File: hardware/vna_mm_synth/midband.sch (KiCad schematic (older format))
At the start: 6 parts

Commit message: added power supply sequencing
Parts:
- gave numbers to parts that had none: 6
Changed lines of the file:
@@
 $EndDescr
 $Comp
-L maam-011101:MAAM-011101 U?
+L maam-011101:MAAM-011101 U601
 U 1 1 5D2874FF
 P 3650 3850
-F 0 "U?" V 4100 4100 60  0000 C CNN
+F 0 "U601" V 4100 4100 60  0000 C CNN
 F 1 "MAAM-011101" V 4000 4350 60  0000 C CNN
 F 2 "" H 3800 3750 60  0000 C CNN
@@
 $EndComp
 $Comp
-L power:GND #PWR?
+L power:GND #PWR0148
 U 1 1 5D2E3704
 P 3100 3850
-F 0 "#PWR?" H 3100 3600 50  0001 C CNN
+F 0 "#PWR0148" H 3100 3600 50  0001 C CNN
 F 1 "GND" H 3105 3677 50  0000 C CNN
 F 2 "" H 3100 3850 50  0001 C CNN
@@
 	3100 3850 3200 3850
 $Comp
-L power:GND #PWR?
+L power:GND #PWR0149
 U 1 1 5D2FD268
 P 3650 3300
-F 0 "#PWR?" H 3650 3050 50  0001 C CNN
+F 0 "#PWR0149" H 3650 3050 50  0001 C CNN
 F 1 "GND" H 3655 3127 50  0000 C CNN
 F 2 "" H 3650 3300 50  0001 C CNN
@@
 	3550 3350 3550 3400
 $Comp
-L power:GND #PWR?
+L power:GND #PWR0150
 U 1 1 5D2FE136
 P 3650 4400
-F 0 "#PWR?" H 3650 4150 50  0001 C CNN
+F 0 "#PWR0150" H 3650 4150 50  0001 C CNN
 F 1 "GND" H 3655 4227 50  0000 C CNN
 F 2 "" H 3650 4400 50  0001 C CNN
@@
 	3550 4300 3550 4400
 $Comp
-L Device:L_Small L?
+L Device:L_Small L601
 U 1 1 5D2FEAD5
 P 4550 3900
-F 0 "L?" H 4598 3946 50  0000 L CNN
+F 0 "L601" H 4598 3946 50  0000 L CNN
 F 1 "BLM15GG471" H 4598 3855 50  0000 L CNN
 F 2 "" H 4550 3900 50  0001 C CNN
@@
 INTERNAL DC BLOCK\nON RFin
 $Comp
-L Device:C_Small C?
+L Device:C_Small C601
 U 1 1 5D2FFB44
 P 5100 4400
-F 0 "C?" V 4871 4400 50  0000 C CNN
+F 0 "C601" V 4871 4400 50  0000 C CNN
 F 1 "100 pF" V 4962 4400 50  0000 C CNN
 F 2 "" H 5100 4400 50  0001 C CNN
@@
 Connection ~ 4550 4400
 $Comp
-L Device:C_Small C?
+L Device:C_Small C602
 U 1 1 5D3002AC
 P 5150 3450
-F 0 "C?" H 5058 3404 50  0000 R CNN
+F 0 "C602" H 5058 3404 50  0000 R CNN
 F 1 "100 pF" H 5058 3495 50  0000 R CNN
 F 2 "" H 5150 3450 50  0001 C CNN
@@
 $EndComp
 $Comp
-L Device:C_Small C?
+L Device:C_Small C603
 U 1 1 5D301255
 P 5600 3450
-F 0 "C?" H 5508 3404 50  0000 R CNN
+F 0 "C603" H 5508 3404 50  0000 R CNN
 F 1 "100 nF" H 5508 3495 50  0000 R CNN
 F 2 "" H 5600 3450 50  0001 C CNN
@@
 $EndComp
 $Comp
-L Device:C_Small C?
+L Device:C_Small C604
 U 1 1 5D3015C8
 P 6050 3450
-F 0 "C?" H 5958 3404 50  0000 R CNN
+F 0 "C604" H 5958 3404 50  0000 R CNN
 F 1 "2.2 uF" H 5958 3495 50  0000 R CNN
 F 2 "" H 6050 3450 50  0001 C CNN
@@
 $EndComp
 $Comp
-L power:GND #PWR?
+L power:GND #PWR0151
 U 1 1 5D301FA8
 P 5150 3600
-F 0 "#PWR?" H 5150 3350 50  0001 C CNN
+F 0 "#PWR0151" H 5150 3350 50  0001 C CNN
 F 1 "GND" H 5155 3427 50  0000 C CNN
 F 2 "" H 5150 3600 50  0001 C CNN
@@
 	5150 3550 5150 3600
 $Comp
-L power:GND #PWR?
+L power:GND #PWR0152
 U 1 1 5D30289B
 P 5600 3600
-F 0 "#PWR?" H 5600 3350 50  0001 C CNN
+F 0 "#PWR0152" H 5600 3350 50  0001 C CNN
 F 1 "GND" H 5605 3427 50  0000 C CNN
 F 2 "" H 5600 3600 50  0001 C CNN
@@
 	5600 3550 5600 3600
 $Comp
-L power:GND #PWR?
+L power:GND #PWR0153
 U 1 1 5D302DE5
 P 6050 3600
-F 0 "#PWR?" H 6050 3350 50  0001 C CNN
+F 0 "#PWR0153" H 6050 3350 50  0001 C CNN
 F 1 "GND" H 6055 3427 50  0000 C CNN
 F 2 "" H 6050 3600 50  0001 C CNN

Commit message: added trl cal and set of breakout boards
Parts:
- C601, C602, C603: footprint (none) -> Capacitors_SMD:C_0402
- C604: footprint (none) -> Capacitors_SMD:C_0603
- L601: footprint (none) -> Resistors_SMD:R_0402
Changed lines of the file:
@@
 F 0 "U601" V 4100 4100 60  0000 C CNN
 F 1 "MAAM-011101" V 4000 4350 60  0000 C CNN
-F 2 "" H 3800 3750 60  0000 C CNN
+F 2 "" H 3800 3750 60  0001 C CNN
 F 3 "" H 3800 3750 60  0000 C CNN
 	1    3650 3850
@@
 $EndComp
 $Comp
-L power:GND #PWR0148
+L power:GND #PWR0601
 U 1 1 5D2E3704
 P 3100 3850
-F 0 "#PWR0148" H 3100 3600 50  0001 C CNN
+F 0 "#PWR0601" H 3100 3600 50  0001 C CNN
 F 1 "GND" H 3105 3677 50  0000 C CNN
 F 2 "" H 3100 3850 50  0001 C CNN
@@
 	3100 3850 3200 3850
 $Comp
-L power:GND #PWR0149
+L power:GND #PWR0602
 U 1 1 5D2FD268
 P 3650 3300
-F 0 "#PWR0149" H 3650 3050 50  0001 C CNN
+F 0 "#PWR0602" H 3650 3050 50  0001 C CNN
 F 1 "GND" H 3655 3127 50  0000 C CNN
 F 2 "" H 3650 3300 50  0001 C CNN
@@
 	3550 3350 3550 3400
 $Comp
-L power:GND #PWR0150
+L power:GND #PWR0603
 U 1 1 5D2FE136
 P 3650 4400
-F 0 "#PWR0150" H 3650 4150 50  0001 C CNN
+F 0 "#PWR0603" H 3650 4150 50  0001 C CNN
 F 1 "GND" H 3655 4227 50  0000 C CNN
 F 2 "" H 3650 4400 50  0001 C CNN
@@
 F 0 "L601" H 4598 3946 50  0000 L CNN
 F 1 "BLM15GG471" H 4598 3855 50  0000 L CNN
-F 2 "" H 4550 3900 50  0001 C CNN
+F 2 "Resistors_SMD:R_0402" H 4550 3900 50  0001 C CNN
 F 3 "~" H 4550 3900 50  0001 C CNN
 	1    4550 3900
@@
 F 0 "C601" V 4871 4400 50  0000 C CNN
 F 1 "100 pF" V 4962 4400 50  0000 C CNN
-F 2 "" H 5100 4400 50  0001 C CNN
+F 2 "Capacitors_SMD:C_0402" H 5100 4400 50  0001 C CNN
 F 3 "~" H 5100 4400 50  0001 C CNN
 	1    5100 4400
@@
 F 0 "C602" H 5058 3404 50  0000 R CNN
 F 1 "100 pF" H 5058 3495 50  0000 R CNN
-F 2 "" H 5150 3450 50  0001 C CNN
+F 2 "Capacitors_SMD:C_0402" H 5150 3450 50  0001 C CNN
 F 3 "~" H 5150 3450 50  0001 C CNN
 	1    5150 3450
@@
 F 0 "C603" H 5508 3404 50  0000 R CNN
 F 1 "100 nF" H 5508 3495 50  0000 R CNN
-F 2 "" H 5600 3450 50  0001 C CNN
+F 2 "Capacitors_SMD:C_0402" H 5600 3450 50  0001 C CNN
 F 3 "~" H 5600 3450 50  0001 C CNN
 	1    5600 3450
@@
 F 0 "C604" H 5958 3404 50  0000 R CNN
 F 1 "2.2 uF" H 5958 3495 50  0000 R CNN
-F 2 "" H 6050 3450 50  0001 C CNN
+F 2 "Capacitors_SMD:C_0603" H 6050 3450 50  0001 C CNN
 F 3 "~" H 6050 3450 50  0001 C CNN
 	1    6050 3450
@@
 $EndComp
 $Comp
-L power:GND #PWR0151
+L power:GND #PWR0604
 U 1 1 5D301FA8
 P 5150 3600
-F 0 "#PWR0151" H 5150 3350 50  0001 C CNN
+F 0 "#PWR0604" H 5150 3350 50  0001 C CNN
 F 1 "GND" H 5155 3427 50  0000 C CNN
 F 2 "" H 5150 3600 50  0001 C CNN
@@
 	5150 3550 5150 3600
 $Comp
-L power:GND #PWR0152
+L power:GND #PWR0605
 U 1 1 5D30289B
 P 5600 3600
-F 0 "#PWR0152" H 5600 3350 50  0001 C CNN
+F 0 "#PWR0605" H 5600 3350 50  0001 C CNN
 F 1 "GND" H 5605 3427 50  0000 C CNN
 F 2 "" H 5600 3600 50  0001 C CNN
@@
 	5600 3550 5600 3600
 $Comp
-L power:GND #PWR0153
+L power:GND #PWR0606
 U 1 1 5D302DE5
 P 6050 3600
-F 0 "#PWR0153" H 6050 3350 50  0001 C CNN
+F 0 "#PWR0606" H 6050 3350 50  0001 C CNN
 F 1 "GND" H 6055 3427 50  0000 C CNN
 F 2 "" H 6050 3600 50  0001 C CNN

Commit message: fixed mirrored 3.3V regulator on sequencer board, created and assigned footprints for synth
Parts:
- U601: footprint (none) -> vna_mm:TDFN6
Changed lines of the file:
@@
 F 0 "U601" V 4100 4100 60  0000 C CNN
 F 1 "MAAM-011101" V 4000 4350 60  0000 C CNN
-F 2 "" H 3800 3750 60  0001 C CNN
+F 2 "vna_mm:TDFN6" H 3800 3750 60  0001 C CNN
 F 3 "" H 3800 3750 60  0000 C CNN
 	1    3650 3850

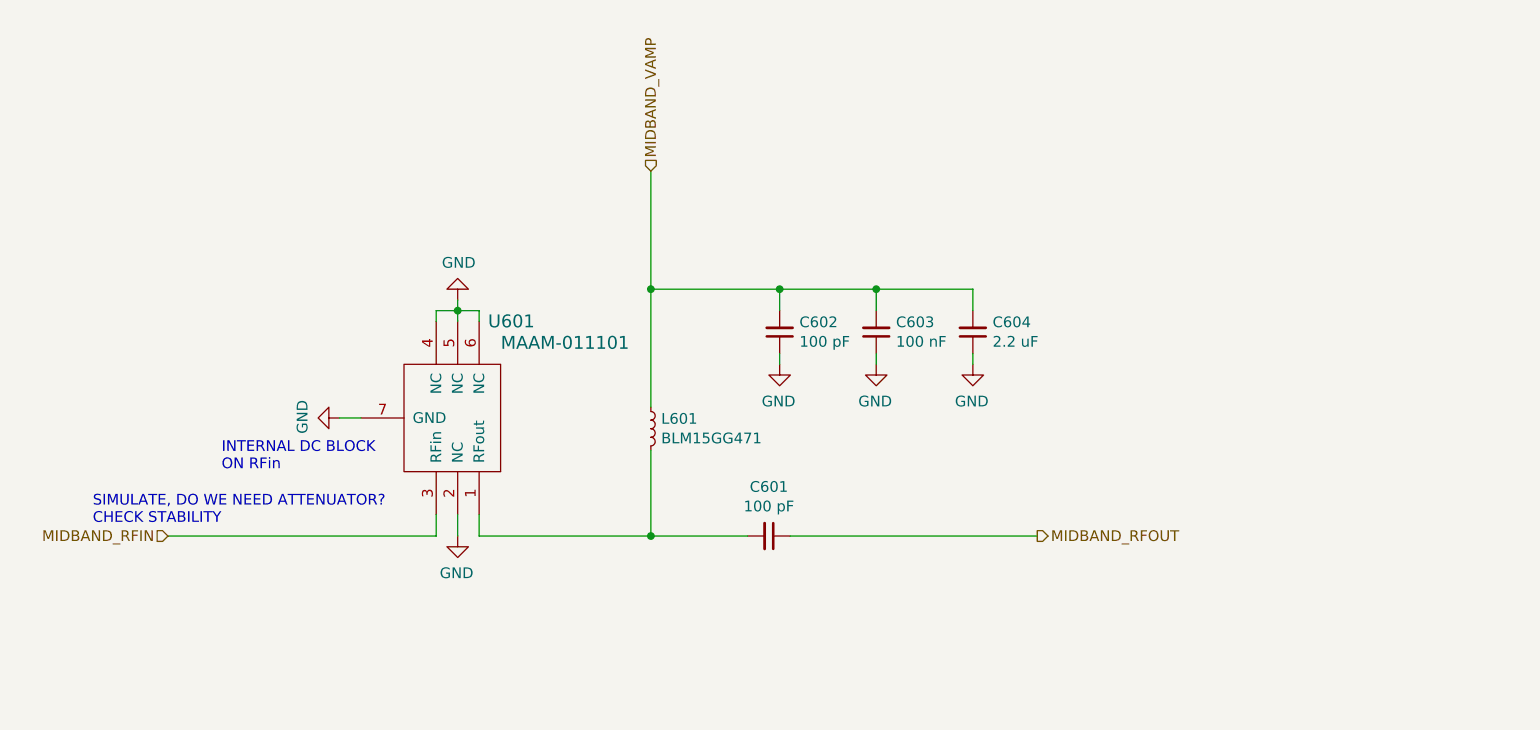
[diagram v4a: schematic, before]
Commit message: started separate reference clock generation board
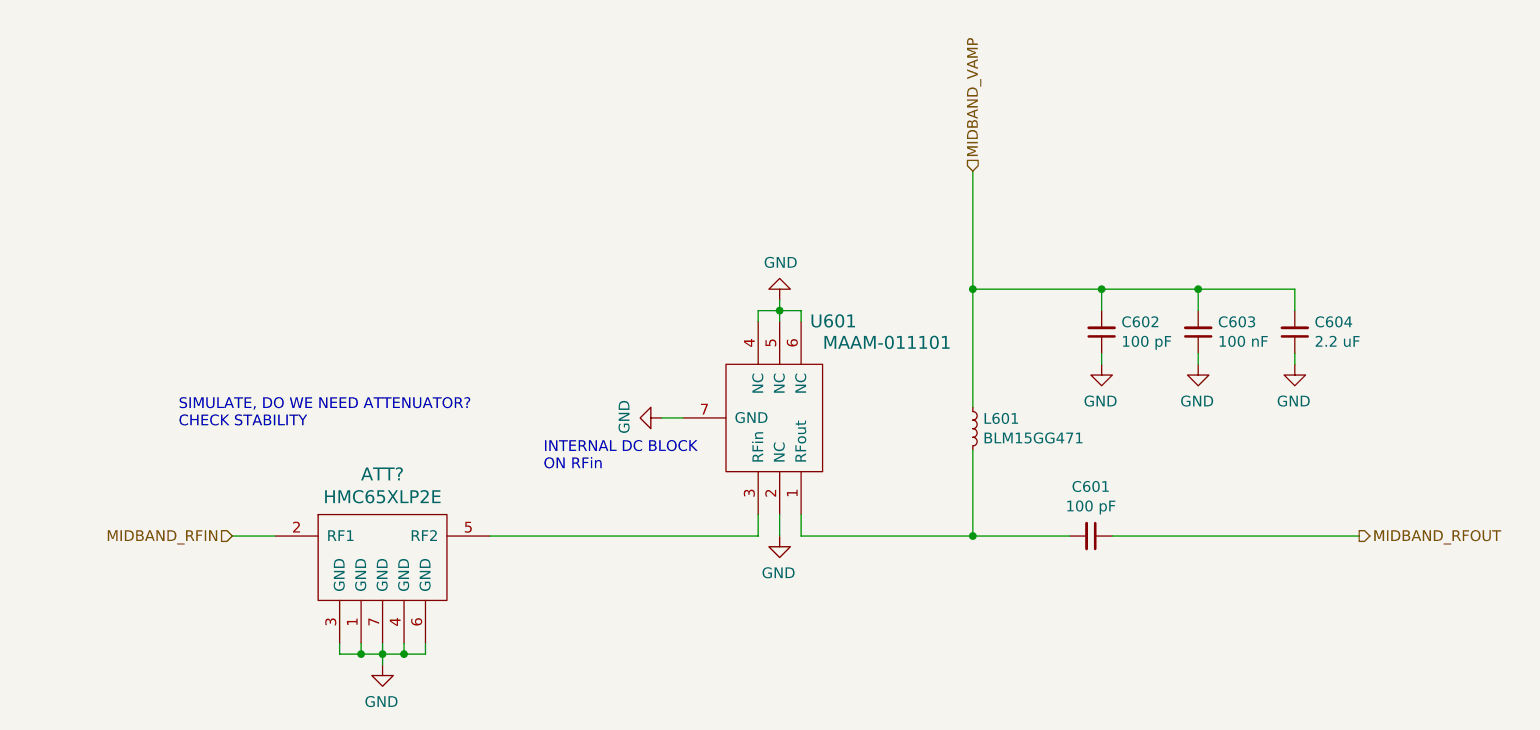
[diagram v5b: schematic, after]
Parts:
- added ATT?: HMC65XLP2E, vna_mm:LP2E_DFN6_2x2mm_Pitch0.60mm, symbol vna_mm:HMC65XLP2E
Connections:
- net GND: now also ATT?.1 (GND), ATT?.3 (GND), ATT?.4 (GND), ATT?.6 (GND), ATT?.7 (GND)
- net MIDBAND_RFIN: now also ATT?.2 (RF1); no longer U601.3 (RFin)
- new net: ATT?.5 (RF2), U601.3 (RFin)
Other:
- moved on the sheet: C601, C602, C603, C604, L601, U601

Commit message: cleanup and update vna mm synth schematic for modern kicad libraries
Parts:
- C601, C602, C603: footprint Capacitors_SMD:C_0402 -> Capacitor_SMD:C_0402_1005Metric
- C604: footprint Capacitors_SMD:C_0603 -> Capacitor_SMD:C_0603_1608Metric
- L601: footprint Resistors_SMD:R_0402 -> Inductor_SMD:L_0402_1005Metric
- U601: symbol maam-011101:MAAM-011101 -> vna_mm:MAAM-011101
- gave numbers to parts that had none: 1
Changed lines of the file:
@@
 $Descr A4 11693 8268
 encoding utf-8
-Sheet 6 12
+Sheet 6 11
 Title ""
 Date ""
@@
 $EndDescr
 $Comp
-L maam-011101:MAAM-011101 U601
+L vna_mm:MAAM-011101 U601
 U 1 1 5D2874FF
 P 5150 3850
@@
 F 0 "L601" H 6098 3946 50  0000 L CNN
 F 1 "BLM15GG471" H 6098 3855 50  0000 L CNN
-F 2 "Resistors_SMD:R_0402" H 6050 3900 50  0001 C CNN
+F 2 "Inductor_SMD:L_0402_1005Metric" H 6050 3900 50  0001 C CNN
 F 3 "~" H 6050 3900 50  0001 C CNN
 	1    6050 3900
@@
 F 0 "C601" V 6371 4400 50  0000 C CNN
 F 1 "100 pF" V 6462 4400 50  0000 C CNN
-F 2 "Capacitors_SMD:C_0402" H 6600 4400 50  0001 C CNN
+F 2 "Capacitor_SMD:C_0402_1005Metric" H 6600 4400 50  0001 C CNN
 F 3 "~" H 6600 4400 50  0001 C CNN
 	1    6600 4400
@@
 F 0 "C602" H 6558 3404 50  0000 R CNN
 F 1 "100 pF" H 6558 3495 50  0000 R CNN
-F 2 "Capacitors_SMD:C_0402" H 6650 3450 50  0001 C CNN
+F 2 "Capacitor_SMD:C_0402_1005Metric" H 6650 3450 50  0001 C CNN
 F 3 "~" H 6650 3450 50  0001 C CNN
 	1    6650 3450
@@
 F 0 "C603" H 7008 3404 50  0000 R CNN
 F 1 "100 nF" H 7008 3495 50  0000 R CNN
-F 2 "Capacitors_SMD:C_0402" H 7100 3450 50  0001 C CNN
+F 2 "Capacitor_SMD:C_0402_1005Metric" H 7100 3450 50  0001 C CNN
 F 3 "~" H 7100 3450 50  0001 C CNN
 	1    7100 3450
@@
 F 0 "C604" H 7458 3404 50  0000 R CNN
 F 1 "2.2 uF" H 7458 3495 50  0000 R CNN
-F 2 "Capacitors_SMD:C_0603" H 7550 3450 50  0001 C CNN
+F 2 "Capacitor_SMD:C_0603_1608Metric" H 7550 3450 50  0001 C CNN
 F 3 "~" H 7550 3450 50  0001 C CNN
 	1    7550 3450
@@
 	6700 4400 7850 4400
 $Comp
-L vna_mm:HMC65XLP2E ATT?
+L vna_mm:HMC65XLP2E ATT601
 U 1 1 5E2708FD
 P 3300 4400
-F 0 "ATT?" H 3300 4687 60  0000 C CNN
+F 0 "ATT601" H 3300 4687 60  0000 C CNN
 F 1 "HMC65XLP2E" H 3300 4581 60  0000 C CNN
 F 2 "vna_mm:LP2E_DFN6_2x2mm_Pitch0.60mm" H 3000 4600 60  0001 C CNN
@@
 	2600 4400 2800 4400
 $Comp
-L power:GND #PWR?
+L power:GND #PWR0105
 U 1 1 5E271C06
 P 3300 5000
-F 0 "#PWR?" H 3300 4750 50  0001 C CNN
+F 0 "#PWR0105" H 3300 4750 50  0001 C CNN
 F 1 "GND" H 3305 4827 50  0000 C CNN
 F 2 "" H 3300 5000 50  0001 C CNN
